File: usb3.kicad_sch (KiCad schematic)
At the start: 50 parts, among them J5 WE_632723300011_alt_symbol, Q19 PJE138K, Q4 PJE138K, U17 HD3SS3220, U18 AP22615, U19 TPD4E05U06QDQARQ1, U20 TPD4E05U06QDQARQ1, U21 TPD4E05U06QDQARQ1

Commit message: Renaming Sheets
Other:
- company: Antmicro Ltd -> Dronolab
- title: Jetson Orin Baseboard -> USB3
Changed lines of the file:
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@@
   (paper "A3")
   (title_block
-    (title "Jetson Orin Baseboard")
-    (date "2023-03-03")
-    (rev "1.1.0")
-    (company "Antmicro Ltd")
-    (comment 1 "www.antmicro.com")
+    (title "USB3")
+    (date "2023-07-05")
+    (rev "1.0.0")
+    (company "Dronolab")
+    (comment 1 "dronolab.etsmtl.ca")
   )
   (junction (at 270.51 87.63) (diameter 0) (color 0 0 0 0)

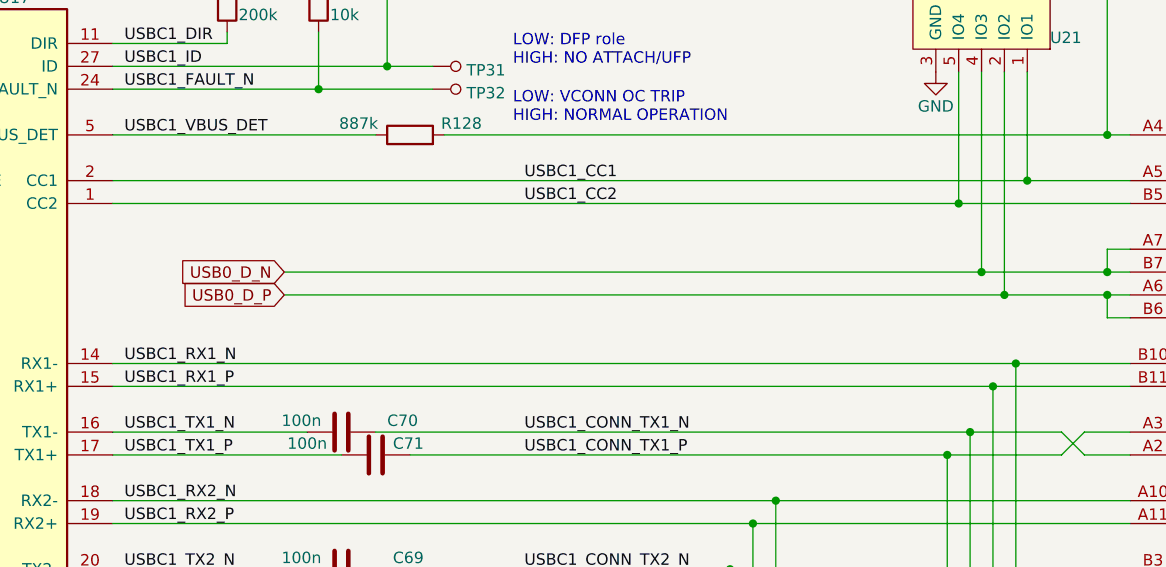
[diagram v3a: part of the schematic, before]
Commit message: Merge du usb-c debug et usb-c 1 et suppression de usb-c 3
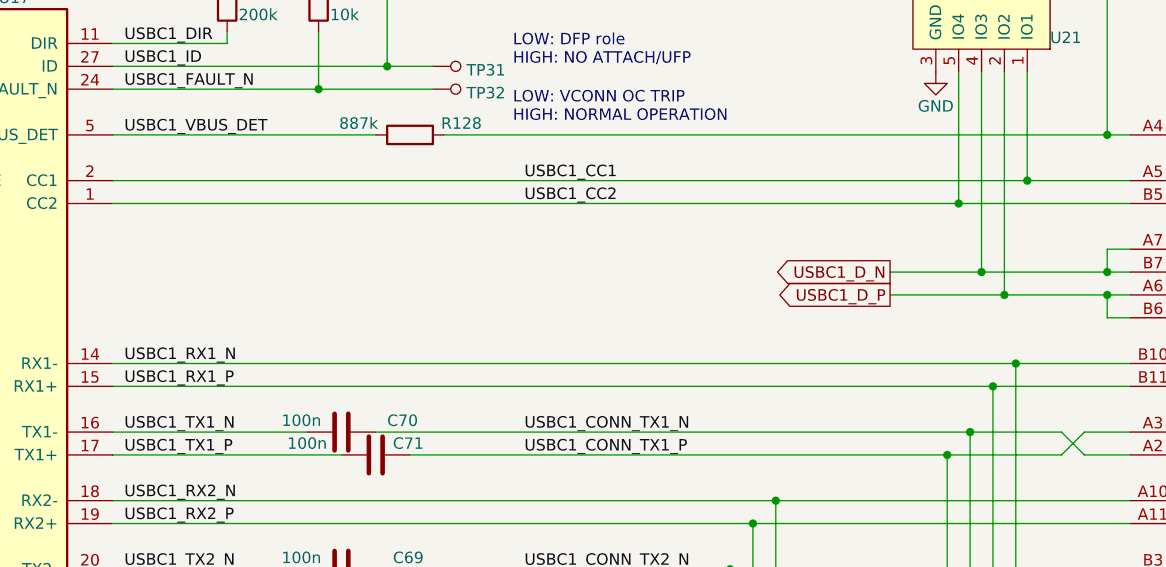
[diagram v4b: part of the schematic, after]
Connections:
- net USB0_D_N renamed USBC1_D_N
- net USB0_D_P renamed USBC1_D_P
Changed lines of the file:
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@@
   (junction (at 339.725 78.74) (diameter 0) (color 0 0 0 0)
   )
+  (junction (at 275.59 147.32) (diameter 0) (color 0 0 0 0)
+  )
   (junction (at 165.1 97.79) (diameter 0) (color 0 0 0 0)
   )
@@
   (junction (at 207.01 102.87) (diameter 0) (color 0 0 0 0)
   )
+  (junction (at 273.05 144.78) (diameter 0) (color 0 0 0 0)
+  )
   (junction (at 247.65 172.72) (diameter 0) (color 0 0 0 0)
   )
@@
   (junction (at 274.32 157.48) (diameter 0) (color 0 0 0 0)
   )
-  (junction (at 273.05 144.78) (diameter 0) (color 0 0 0 0)
-  )
   (junction (at 287.02 144.78) (diameter 0) (color 0 0 0 0)
   )
@@
   )
   (junction (at 207.01 121.92) (diameter 0) (color 0 0 0 0)
-  )
-  (junction (at 275.59 147.32) (diameter 0) (color 0 0 0 0)
   )
   (junction (at 250.19 170.18) (diameter 0) (color 0 0 0 0)
@@
     (stroke (width 0) (type default))
   )
-  (wire (pts (xy 195.58 144.78) (xy 273.05 144.78))
-    (stroke (width 0) (type default))
-  )
   (wire (pts (xy 250.19 87.63) (xy 270.51 87.63))
     (stroke (width 0) (type default))
@@
     (stroke (width 0) (type default))
   )
-  (wire (pts (xy 195.58 147.32) (xy 275.59 147.32))
-    (stroke (width 0) (type default))
-  )
   (wire (pts (xy 355.6 81.28) (xy 355.6 88.265))
     (stroke (width 0) (type default))
@@
     (stroke (width 0) (type default))
   )
+  (wire (pts (xy 262.89 144.78) (xy 273.05 144.78))
+    (stroke (width 0) (type default))
+  )
   (wire (pts (xy 143.51 137.16) (xy 107.95 137.16))
     (stroke (width 0) (type default))
@@
   )
   (wire (pts (xy 269.24 165.1) (xy 269.24 185.42))
+    (stroke (width 0) (type default))
+  )
+  (wire (pts (xy 262.89 147.32) (xy 275.59 147.32))
     (stroke (width 0) (type default))
   )
@@
     )
   )
+  (global_label "USBC1_D_P" (shape output) (at 262.89 147.32 180) (fields_autoplaced)
+    (effects (font (size 1.27 1.27)) (justify right))
+    (property "Intersheetrefs" "${INTERSHEET_REFS}" (at 249.1401 147.32 0)
+      (effects (font (size 1.27 1.27)) (justify right))
+    )
+  )
   (global_label "SYS_SCL" (shape input) (at 107.95 175.26 180)
     (effects (font (size 1.27 1.27)) (justify right))
@@
     )
   )
-  (global_label "USB0_D_N" (shape input) (at 195.58 144.78 180)
-    (effects (font (size 1.27 1.27)) (justify right))
-    (property "Intersheetrefs" "${INTERSHEET_REFS}" (at 182.245 144.78 0)
-      (effects (font (size 1.27 1.27)) (justify right))
-    )
-  )
   (global_label "USBSS2_TX_N" (shape input) (at 95.25 162.56 180)
     (effects (font (size 1.27 1.27)) (justify right))
@@
     )
   )
-  (global_label "USB0_D_P" (shape input) (at 195.58 147.32 180)
-    (effects (font (size 1.27 1.27)) (justify right))
-    (property "Intersheetrefs" "${INTERSHEET_REFS}" (at 182.245 147.32 0)
-      (effects (font (size 1.27 1.27)) (justify right))
-    )
-  )
   (global_label "USBSS2_RX_P" (shape output) (at 95.25 157.48 180)
     (effects (font (size 1.27 1.27)) (justify right))
@@
     )
   )
+  (global_label "USBC1_D_N" (shape output) (at 262.89 144.78 180) (fields_autoplaced)
+    (effects (font (size 1.27 1.27)) (justify right))
+    (property "Intersheetrefs" "${INTERSHEET_REFS}" (at 249.0796 144.78 0)
+      (effects (font (size 1.27 1.27)) (justify right))
+    )
+  )

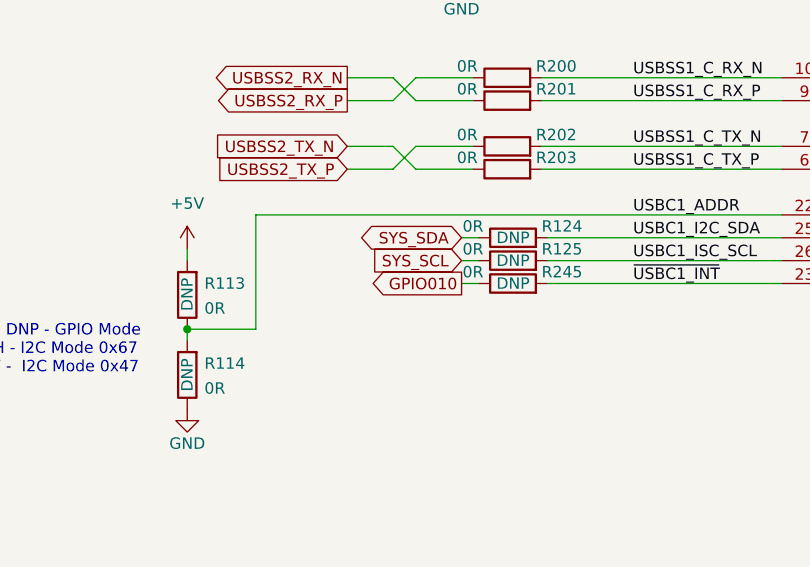
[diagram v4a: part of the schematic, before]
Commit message: Schematic check
Include Pinmux and Schematic Check excels in doc folder and doing a lot of checking and correcting things.
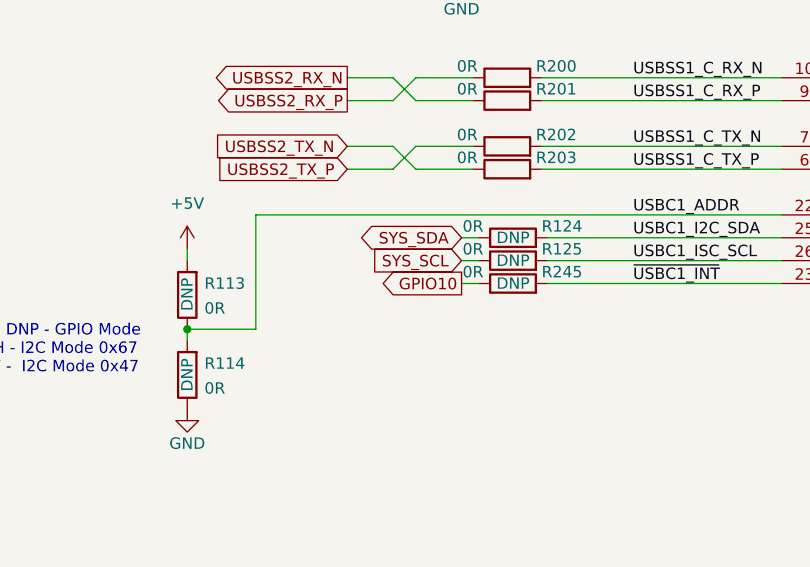
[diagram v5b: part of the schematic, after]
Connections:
- net GPIO010 renamed GPIO10
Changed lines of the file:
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@@
     (effects (font (size 1.27 1.27)) (justify left bottom))
   )
-  (global_label "GPIO010" (shape output) (at 107.95 177.8 180)
+  (global_label "GPIO10" (shape output) (at 107.95 177.8 180)
     (effects (font (size 1.27 1.27)) (justify right))
     (property "Intersheetrefs" "${INTERSHEET_REFS}" (at 86.36 177.8 0)

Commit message: Small changes
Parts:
- added C86, C87: 47p, symbol Device:C
- added R20, R21: R_27R_0402, jetson-orin-baseboard-footprints:0402-res, symbol jetson-orin-baseboard:R_27R_0402
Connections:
- net GND: now also C86.2, C87.1
- net USBC1_D_N: no longer names the net of J5.A7 (D-), J5.B7 (D-), U21.4 (IO3), U21.7 (IO3)
- net USBC1_D_N: now also C86.1, R21.2
- net USBC1_D_P: no longer names the net of J5.A6 (D+), J5.B6 (D+), U21.2 (IO2), U21.9 (IO2)
- net USBC1_D_P: now also C87.2, R20.2
- new net USB_FTDI_N: R21.1
- new net USB_FTDI_P: R20.1

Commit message: Schematic Done
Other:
- moved on the sheet: C66, C73, C86, C87, R124, R125, R138, R184, R20, R21, R23, R24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

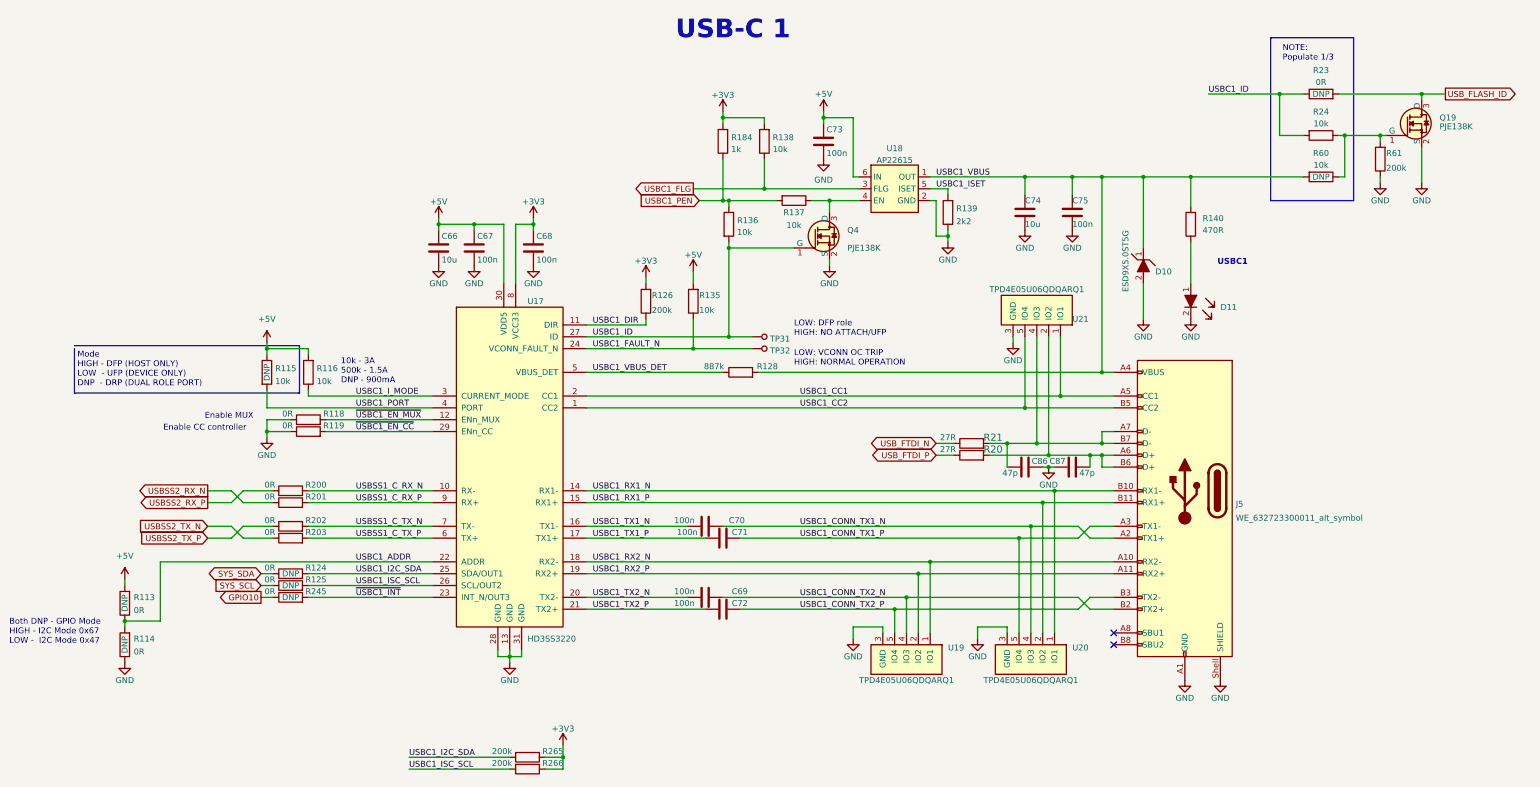
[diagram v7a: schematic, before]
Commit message: Schematic V1 and footprints assigned
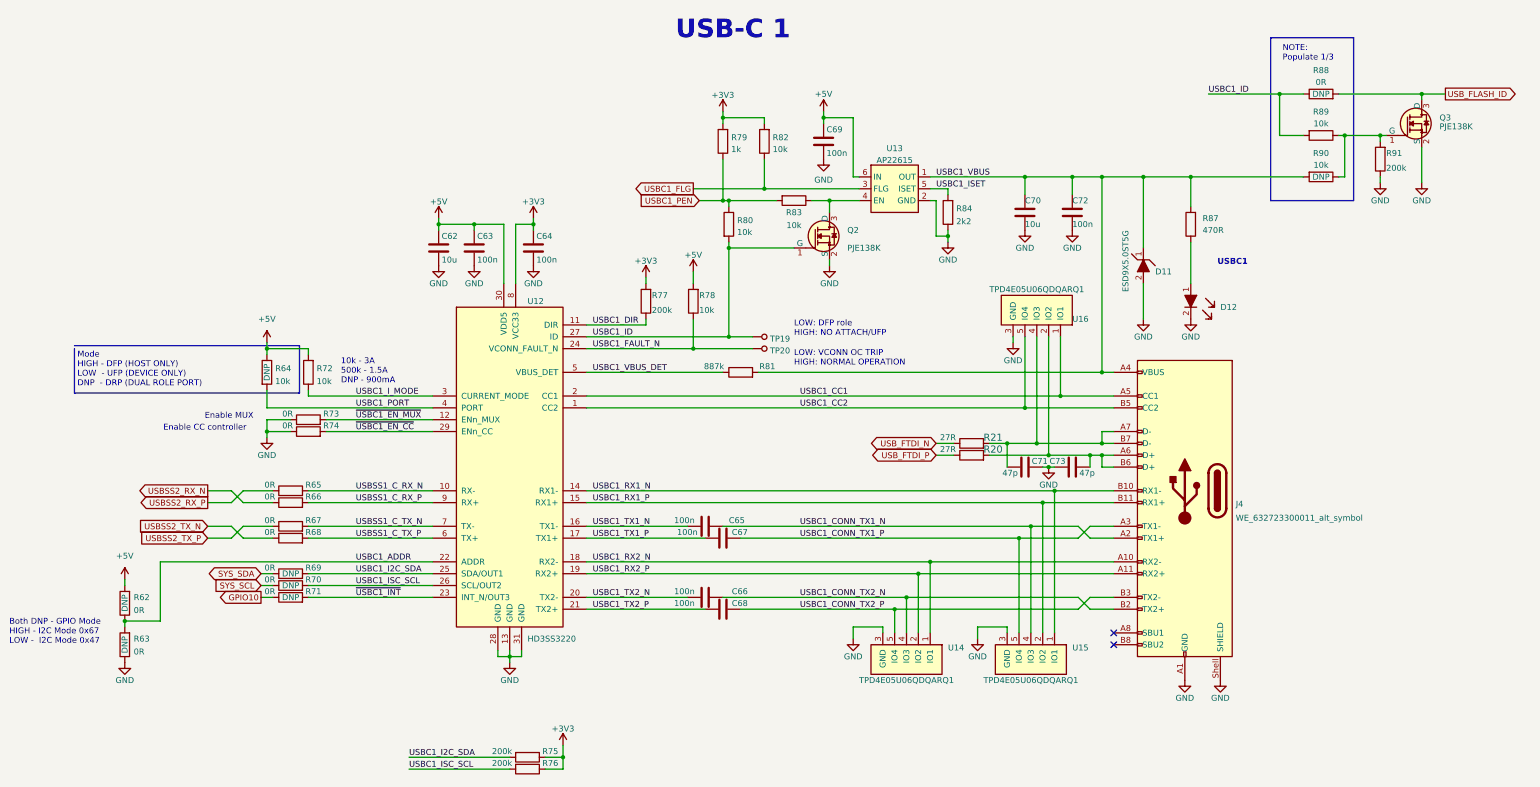
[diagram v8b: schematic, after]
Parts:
- C71: renamed from C86; footprint (none) -> jetson-orin-baseboard-footprints:0402-cap
- C73: renamed from C87; footprint (none) -> jetson-orin-baseboard-footprints:0402-cap
- renumbered C66 to C62, C67 to C63, C68 to C64, C70 to C65, C69 to C66, C71 to C67, C72 to C68, C73 to C69, C74 to C70, C75 to C72, D10 to D11, D11 to D12, J5 to J4, Q4 to Q2, Q19 to Q3, R113 to R62, R114 to R63, R115 to R64, R200 to R65, R201 to R66, R202 to R67, R203 to R68, R124 to R69, R125 to R70, R245 to R71, R116 to R72, R118 to R73, R119 to R74, R265 to R75, R266 to R76, R126 to R77, R135 to R78, R184 to R79, R136 to R80, R128 to R81, R138 to R82, R137 to R83, R139 to R84, R140 to R87, R23 to R88, R24 to R89, R60 to R90, R61 to R91, TP31 to TP19, TP32 to TP20, U17 to U12, U18 to U13, U19 to U14, U20 to U15, U21 to U16
